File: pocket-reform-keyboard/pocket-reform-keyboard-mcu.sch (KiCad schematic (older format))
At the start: 30 parts, among them J1 USB, J2 UART, J3 AUX, SW56 RESET, U1 ATMEGA32U4-AU, U1 MCP1700-3302E_SOT23, Y1 16MHz

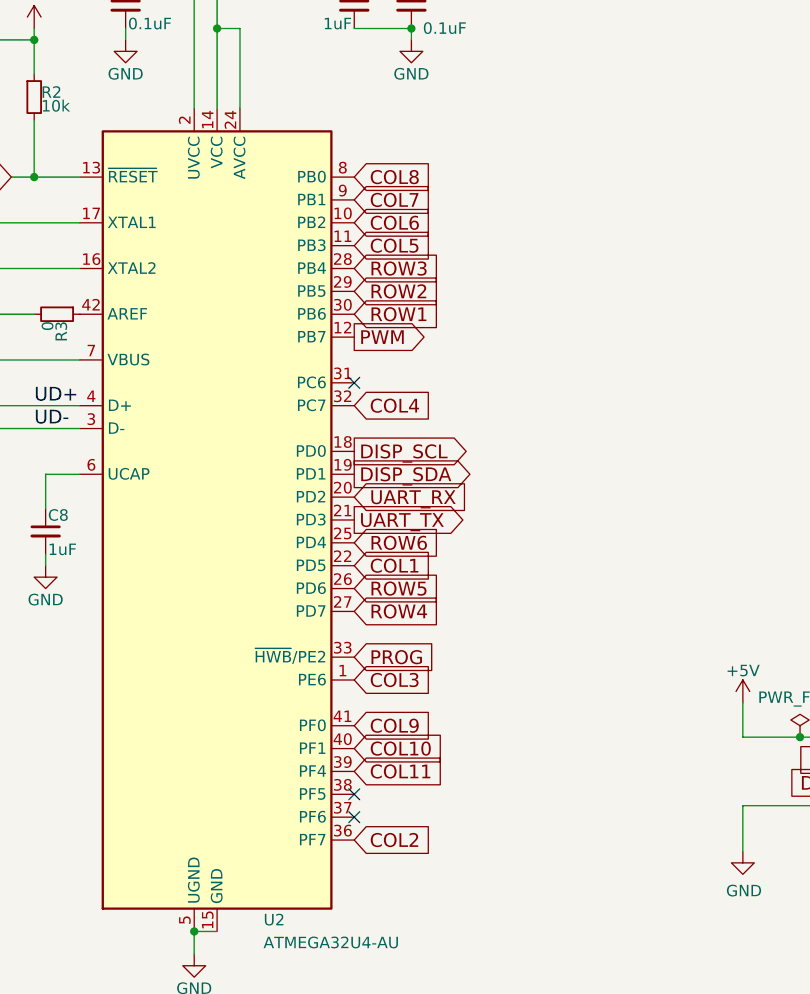
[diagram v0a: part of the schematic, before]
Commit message: keyboard: first routed draft
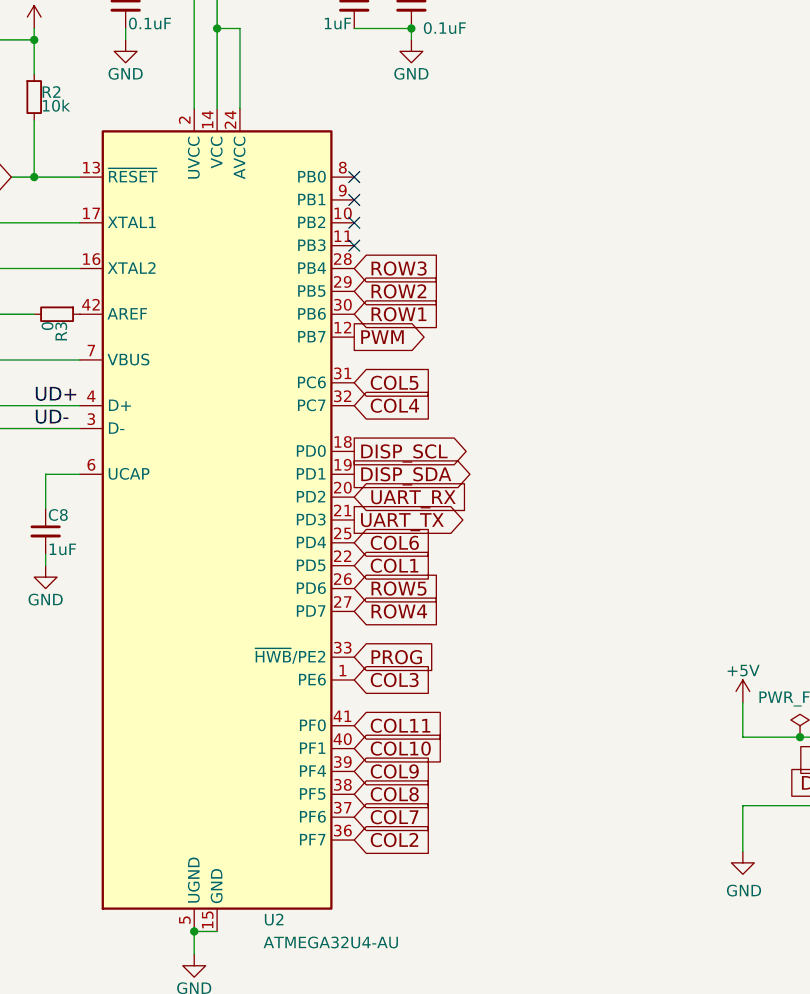
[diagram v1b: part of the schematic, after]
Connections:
- net ROW6 is gone; now on net COL6: U1.25 (PD4)
- net COL11: now also U1.41 (PF0); no longer U1.39 (PF4)
- net COL5: now also U1.31 (PC6); no longer U1.11 (PB3)
- net COL6: no longer U1.10 (PB2)
- net COL7: now also U1.37 (PF6); no longer U1.9 (PB1)
- net COL8: now also U1.38 (PF5); no longer U1.8 (PB0)
- net COL9: now also U1.39 (PF4); no longer U1.41 (PF0)
- no-connect marks 3 -> 4
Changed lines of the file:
@@
 Text GLabel 4450 4900 2    60   Input ~ 0
 ROW5
-Text GLabel 4450 4700 2    60   Input ~ 0
-ROW6
 Text GLabel 4450 4800 2    60   Input ~ 0
 COL1
@@
 Text GLabel 4450 4100 2    60   Input ~ 0
 COL4
-Text GLabel 4450 3400 2    60   Input ~ 0
+Text GLabel 4450 4000 2    60   Input ~ 0
 COL5
-Text GLabel 4450 3300 2    60   Input ~ 0
+Text GLabel 4450 4700 2    60   Input ~ 0
 COL6
-Text GLabel 4450 3200 2    60   Input ~ 0
+Text GLabel 4450 5900 2    60   Input ~ 0
 COL7
-Text GLabel 4450 3100 2    60   Input ~ 0
+Text GLabel 4450 5800 2    60   Input ~ 0
 COL8
-Text GLabel 4450 5500 2    60   Input ~ 0
+Text GLabel 4450 5700 2    60   Input ~ 0
 COL9
 Text GLabel 4450 5600 2    60   Input ~ 0
 COL10
-Text GLabel 4450 5700 2    60   Input ~ 0
+Text GLabel 4450 5500 2    60   Input ~ 0
 COL11
 $Comp
@@
 Wire Wire Line
 	1550 2200 1700 2200
-NoConn ~ 4450 4000
-NoConn ~ 4450 5900
-NoConn ~ 4450 5800
+NoConn ~ 4450 3400
+NoConn ~ 4450 3300
+NoConn ~ 4450 3200
+NoConn ~ 4450 3100
 $EndSCHEMATC

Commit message: keyboard: D-1, sent to fab
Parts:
- removed GFX3: MNT, reform2-keyboard:mntreform-keyboard-badge, symbol Mechanical:MountingHole
- added D56: LED_RGBA, footprints:LED_150080M153000, symbol Device:LED_RGBA
- added R10, R11: 22, Resistor_SMD:R_0603_1608Metric, symbol Device:R_Small
- added R9: 220, Resistor_SMD:R_0603_1608Metric, symbol Device:R_Small
- GFX1: footprint reform2-keyboard:mntreform -> footprints:pocket-reform
- GFX2: footprint reform2-keyboard:mntreform -> footprints:mpre-badge-d1
- H3, H4: footprint MountingHole:MountingHole_2.2mm_M2_Pad -> MountingHole:MountingHole_2.2mm_M2
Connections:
- net +3V3: now also D56.4 (A)
- net at U1.10 (PB2): now also R9.2
- net at U1.11 (PB3): now also R11.2
- net at U1.9 (PB1): now also R10.2
- net PWM: no longer names the net of U1.12 (PB7)
- new net: D56.3 (BK), R11.1
- new net: D56.1 (RK), R9.1
- new net: D56.2 (GK), R10.1
- no-connect marks 4 -> 2
